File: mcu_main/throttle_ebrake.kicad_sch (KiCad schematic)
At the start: 0 parts

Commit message: added throttle and ebrake connectors
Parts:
- added J6: Screw_Terminal_01x03_ebrake, TerminalBlock:TerminalBlock_Xinya_XY308-2.54-3P_1x03_P2.54mm_Horizontal, symbol Connector:Screw_Terminal_01x03
- added J7: Screw_Terminal_01x03_throttle, TerminalBlock:TerminalBlock_Xinya_XY308-2.54-3P_1x03_P2.54mm_Horizontal, symbol Connector:Screw_Terminal_01x03
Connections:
- new net +5V: J6.1 (Pin_1), J7.1 (Pin_1)
- new net GND: J6.3 (Pin_3), J7.3 (Pin_3)
- new net ebrake_sig: J6.2 (Pin_2)
- new net throttle_sig: J7.2 (Pin_2)

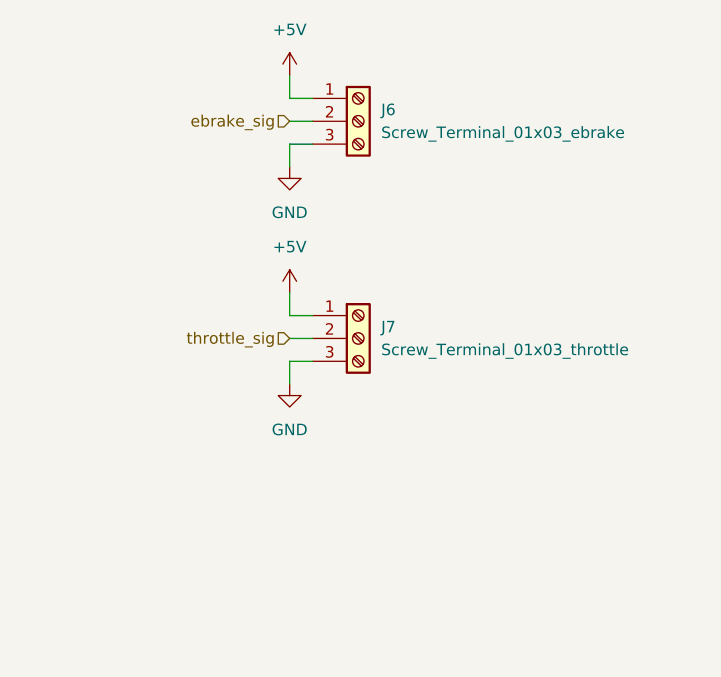
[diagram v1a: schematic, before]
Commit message: added throttle and ebrake connectors
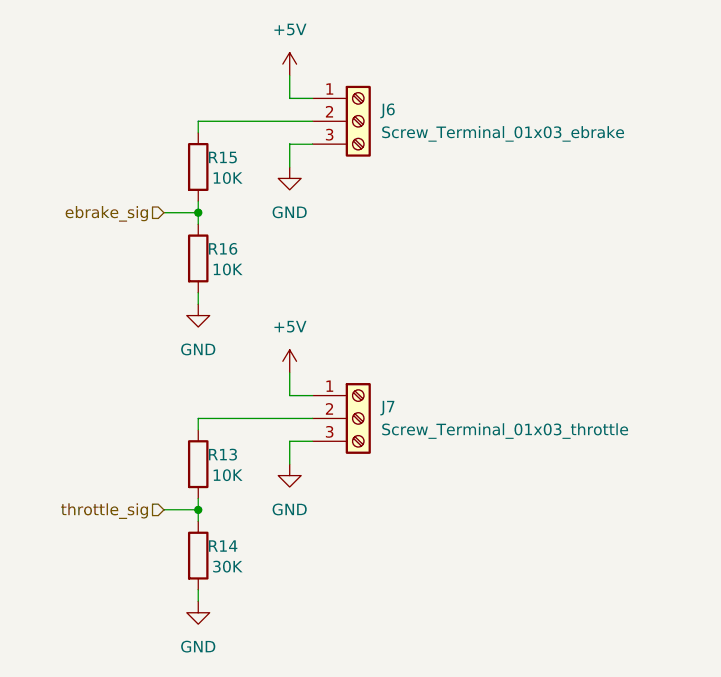
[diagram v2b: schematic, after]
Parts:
- added R13, R15, R16: 10K, Resistor_SMD:R_0805_2012Metric_Pad1.20x1.40mm_HandSolder, symbol Device:R
- added R14: 30K, Resistor_SMD:R_0805_2012Metric_Pad1.20x1.40mm_HandSolder, symbol Device:R
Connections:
- net GND: now also R14.2, R16.2
- net ebrake_sig: now also R15.2, R16.1; no longer J6.2 (Pin_2)
- net throttle_sig: now also R13.2, R14.1; no longer J7.2 (Pin_2)
- new net: J6.2 (Pin_2), R15.1
- new net: J7.2 (Pin_2), R13.1
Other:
- moved on the sheet: J7
